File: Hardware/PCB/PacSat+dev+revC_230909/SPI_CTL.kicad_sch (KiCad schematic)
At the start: 10 parts, among them J801 Conn_02x05_Odd_Even

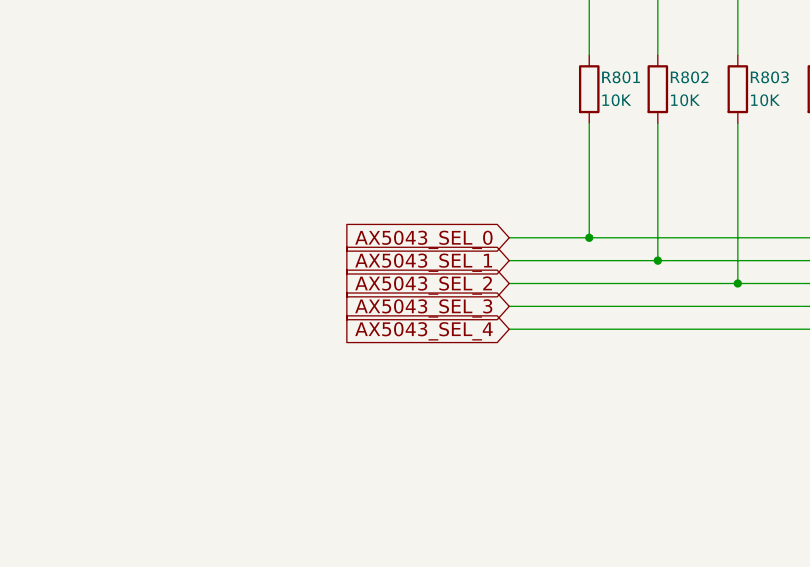
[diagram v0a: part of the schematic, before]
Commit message: Changed schematic to add Select lines for each AX5043 on the CPU.
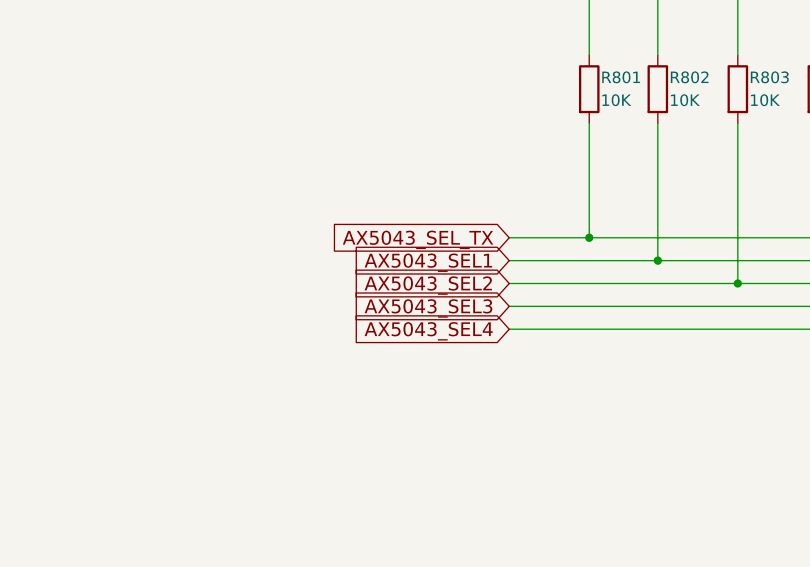
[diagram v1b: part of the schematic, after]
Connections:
- net AX5043_SEL_0 renamed AX5043_SEL_TX
- net AX5043_SEL_1 renamed AX5043_SEL1
- net AX5043_SEL_2 renamed AX5043_SEL2
- net AX5043_SEL_3 renamed AX5043_SEL3
- net AX5043_SEL_4 renamed AX5043_SEL4
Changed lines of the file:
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@@
     (effects (font (size 1.524 1.524)) (justify left bottom))
   )
-  (global_label "AX5043_SEL_0" (shape input) (at 148.59 132.08 180) (fields_autoplaced)
-    (effects (font (size 1.524 1.524)) (justify right))
-    (property "Intersheetrefs" "${INTERSHEET_REFS}" (at 129.4877 132.08 0)
+  (global_label "AX5043_SEL_TX" (shape input) (at 148.59 132.08 180) (fields_autoplaced)
+    (effects (font (size 1.524 1.524)) (justify right))
+    (property "Intersheetrefs" "${INTERSHEET_REFS}" (at 128.2312 132.08 0)
       (effects (font (size 1.524 1.524)) (justify right) hide)
     )
@@
     )
   )
-  (global_label "AX5043_SEL_1" (shape input) (at 148.59 134.62 180) (fields_autoplaced)
-    (effects (font (size 1.524 1.524)) (justify right))
-    (property "Intersheetrefs" "${INTERSHEET_REFS}" (at 129.4877 134.62 0)
-      (effects (font (size 1.524 1.524)) (justify right) hide)
-    )
-  )
-  (global_label "AX5043_SEL_4" (shape input) (at 148.59 142.24 180) (fields_autoplaced)
-    (effects (font (size 1.524 1.524)) (justify right))
-    (property "Intersheetrefs" "${INTERSHEET_REFS}" (at 129.4877 142.24 0)
-      (effects (font (size 1.524 1.524)) (justify right) hide)
-    )
-  )
-  (global_label "AX5043_SEL_3" (shape input) (at 148.59 139.7 180) (fields_autoplaced)
-    (effects (font (size 1.524 1.524)) (justify right))
-    (property "Intersheetrefs" "${INTERSHEET_REFS}" (at 129.4877 139.7 0)
-      (effects (font (size 1.524 1.524)) (justify right) hide)
-    )
-  )
-  (global_label "AX5043_SEL_2" (shape input) (at 148.59 137.16 180) (fields_autoplaced)
-    (effects (font (size 1.524 1.524)) (justify right))
-    (property "Intersheetrefs" "${INTERSHEET_REFS}" (at 129.4877 137.16 0)
+  (global_label "AX5043_SEL1" (shape input) (at 148.59 134.62 180) (fields_autoplaced)
+    (effects (font (size 1.524 1.524)) (justify right))
+    (property "Intersheetrefs" "${INTERSHEET_REFS}" (at 130.5534 134.62 0)
+      (effects (font (size 1.524 1.524)) (justify right) hide)
+    )
+  )
+  (global_label "AX5043_SEL4" (shape input) (at 148.59 142.24 180) (fields_autoplaced)
+    (effects (font (size 1.524 1.524)) (justify right))
+    (property "Intersheetrefs" "${INTERSHEET_REFS}" (at 130.5534 142.24 0)
+      (effects (font (size 1.524 1.524)) (justify right) hide)
+    )
+  )
+  (global_label "AX5043_SEL3" (shape input) (at 148.59 139.7 180) (fields_autoplaced)
+    (effects (font (size 1.524 1.524)) (justify right))
+    (property "Intersheetrefs" "${INTERSHEET_REFS}" (at 130.5534 139.7 0)
+      (effects (font (size 1.524 1.524)) (justify right) hide)
+    )
+  )
+  (global_label "AX5043_SEL2" (shape input) (at 148.59 137.16 180) (fields_autoplaced)
+    (effects (font (size 1.524 1.524)) (justify right))
+    (property "Intersheetrefs" "${INTERSHEET_REFS}" (at 130.5534 137.16 0)
       (effects (font (size 1.524 1.524)) (justify right) hide)
     )
@@
     (pin "1")
     (instances
-      (project "pACsAT_dEV_rEVc_230907"
+      (project "PacSat+dev+revC_230909"
         (path "/cc9f42d2-6985-41ac-acab-5ab7b01c5b38/e22fffe3-8634-4ceb-ab1d-aa069e09a85a"
           (reference "#PWR0802") (unit 1)
@@
     (pin "2")
     (instances
-      (project "pACsAT_dEV_rEVc_230907"
+      (project "PacSat+dev+revC_230909"
         (path "/cc9f42d2-6985-41ac-acab-5ab7b01c5b38/e22fffe3-8634-4ceb-ab1d-aa069e09a85a"
           (reference "R801") (unit 1)
@@
     (pin "2")
     (instances
-      (project "pACsAT_dEV_rEVc_230907"
+      (project "PacSat+dev+revC_230909"
         (path "/cc9f42d2-6985-41ac-acab-5ab7b01c5b38/e22fffe3-8634-4ceb-ab1d-aa069e09a85a"
           (reference "R803") (unit 1)
@@
     (pin "2")
     (instances
-      (project "pACsAT_dEV_rEVc_230907"
+      (project "PacSat+dev+revC_230909"
         (path "/cc9f42d2-6985-41ac-acab-5ab7b01c5b38/e22fffe3-8634-4ceb-ab1d-aa069e09a85a"
           (reference "R808") (unit 1)
@@
     (pin "2")
     (instances
-      (project "pACsAT_dEV_rEVc_230907"
+      (project "PacSat+dev+revC_230909"
         (path "/cc9f42d2-6985-41ac-acab-5ab7b01c5b38/e22fffe3-8634-4ceb-ab1d-aa069e09a85a"
           (reference "R807") (unit 1)
@@
     (pin "1")
     (instances
-      (project "pACsAT_dEV_rEVc_230907"
+      (project "PacSat+dev+revC_230909"
         (path "/cc9f42d2-6985-41ac-acab-5ab7b01c5b38/e22fffe3-8634-4ceb-ab1d-aa069e09a85a"
           (reference "#PWR0728") (unit 1)
@@
     (pin "9")
     (instances
-      (project "pACsAT_dEV_rEVc_230907"
+      (project "PacSat+dev+revC_230909"
         (path "/cc9f42d2-6985-41ac-acab-5ab7b01c5b38/e22fffe3-8634-4ceb-ab1d-aa069e09a85a"
           (reference "J801") (unit 1)
@@
     (pin "2")
     (instances
-      (project "pACsAT_dEV_rEVc_230907"
+      (project "PacSat+dev+revC_230909"
         (path "/cc9f42d2-6985-41ac-acab-5ab7b01c5b38/e22fffe3-8634-4ceb-ab1d-aa069e09a85a"
           (reference "R806") (unit 1)
@@
     (pin "2")
     (instances
-      (project "pACsAT_dEV_rEVc_230907"
+      (project "PacSat+dev+revC_230909"
         (path "/cc9f42d2-6985-41ac-acab-5ab7b01c5b38/e22fffe3-8634-4ceb-ab1d-aa069e09a85a"
           (reference "R805") (unit 1)
@@
     (pin "2")
     (instances
-      (project "pACsAT_dEV_rEVc_230907"
+      (project "PacSat+dev+revC_230909"
         (path "/cc9f42d2-6985-41ac-acab-5ab7b01c5b38/e22fffe3-8634-4ceb-ab1d-aa069e09a85a"
           (reference "R809") (unit 1)
@@
     (pin "2")
     (instances
-      (project "pACsAT_dEV_rEVc_230907"
+      (project "PacSat+dev+revC_230909"
         (path "/cc9f42d2-6985-41ac-acab-5ab7b01c5b38/e22fffe3-8634-4ceb-ab1d-aa069e09a85a"
           (reference "R804") (unit 1)
@@
     (pin "2")
     (instances
-      (project "pACsAT_dEV_rEVc_230907"
+      (project "PacSat+dev+revC_230909"
         (path "/cc9f42d2-6985-41ac-acab-5ab7b01c5b38/e22fffe3-8634-4ceb-ab1d-aa069e09a85a"
           (reference "R802") (unit 1)
